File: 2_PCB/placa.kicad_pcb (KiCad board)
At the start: 2 copper layers, 37 parts, among them J1 Screw_Terminal_01x02, J2 Conn_01x05_Male, J3 Screw_Terminal_01x02, SW1 SW_Push, U1 STM32L051C8Tx, U2 Ai-Thinker-Ra-01, Y1 8 MHz, Y2 32.768 kHz

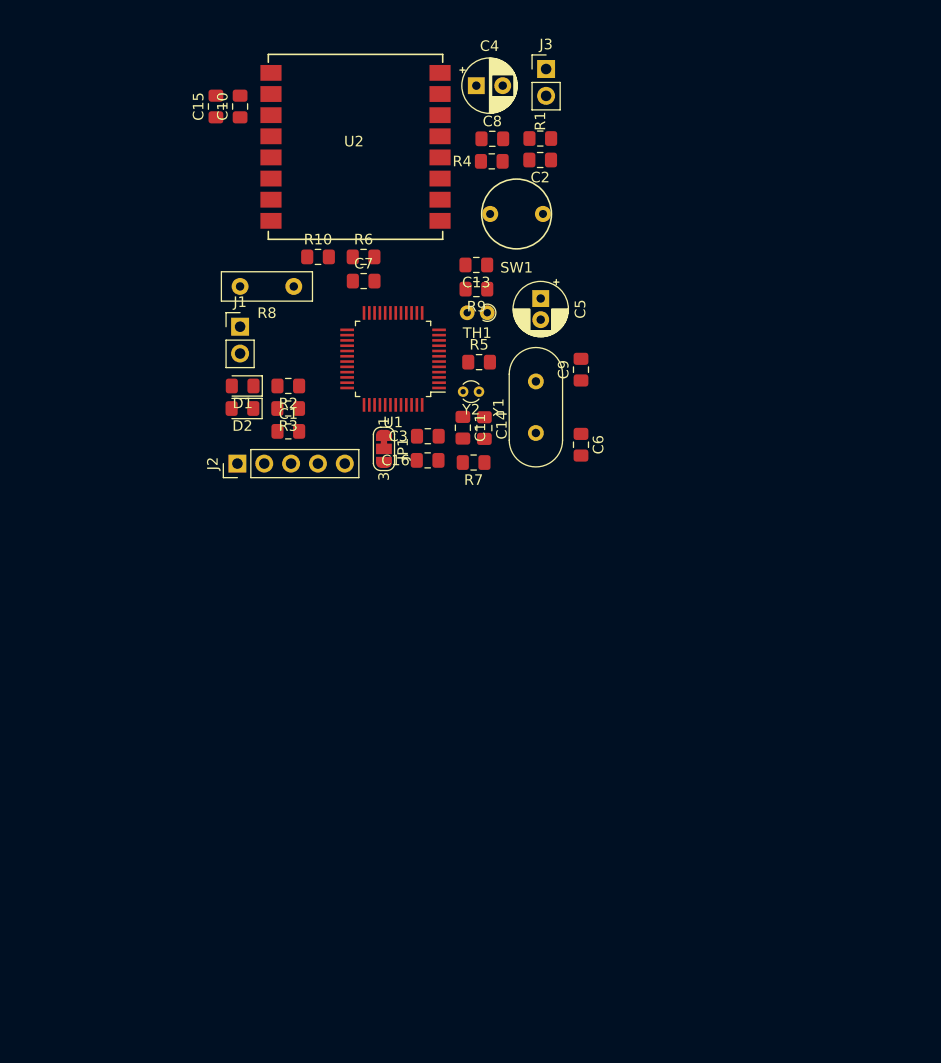
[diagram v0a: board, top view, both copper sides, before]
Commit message: Remap SPI pins, reposition components; start routing
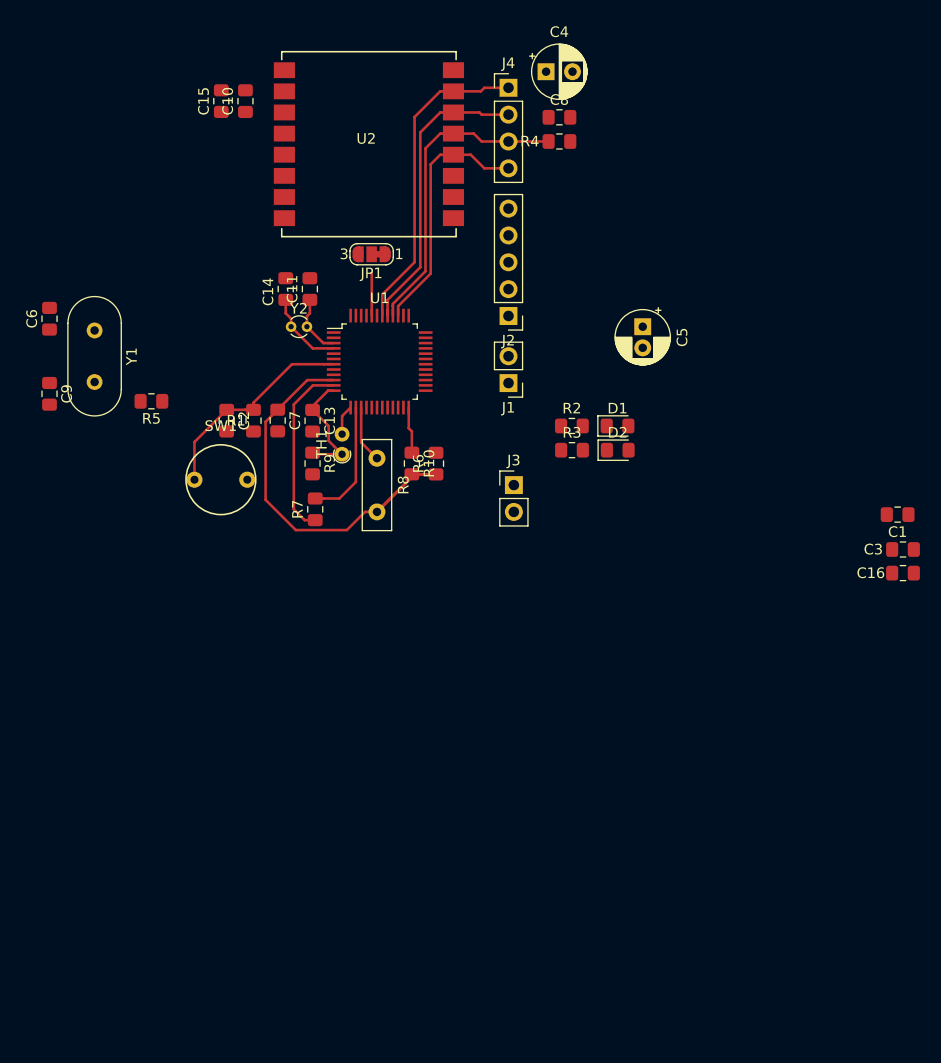
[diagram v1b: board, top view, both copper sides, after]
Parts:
- added J4: TestPoints, Connector_PinHeader_2.54mm:PinHeader_1x04_P2.54mm_Vertical, F.Cu at (138.7, 32.3)
- moved C1 58.2 mm to (175.5, 72.6), turned to 180 degrees
- moved C6 51.7 mm to (95.2, 54.1), turned to 90 degrees
- moved C9 50.3 mm to (95.2, 61.2), turned to 270 degrees
- moved C16 46.2 mm to (176.0, 78.2)
- moved C3 46.2 mm to (176.0, 75.9)
- moved Y1 42.9 mm to (99.5, 55.2), turned to 270 degrees
- moved J3 39.5 mm to (139.2, 69.8)
- moved C2 38.6 mm to (112.0, 63.8), turned to 270 degrees
- moved R1 38.1 mm to (114.6, 63.8), turned to 90 degrees
- moved SW1 37.6 mm to (111.5, 69.3), turned to 180 degrees
- moved D2 35.7 mm to (149.0, 66.5), turned to 0 degrees
- moved D1 35.7 mm to (149.0, 64.3), turned to 0 degrees
- moved R5 31.2 mm to (104.9, 61.9), turned to 180 degrees
- moved J2 29.2 mm to (138.7, 53.8), turned to 180 degrees
- moved R3 27.1 mm to (144.7, 66.5), turned to 0 degrees
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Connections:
- J2 pad 3: /SWCLK -> /NRST
- J2 pad 4: /NRST -> /SWCLK
- U1 pad 10: /ADC_TEMP -> /ADC_RH
- U1 pad 12: /ADC_RH -> /ADC_TEMP
- U1 pad 15: /SPI_SCK -> /PWR_RH
- U1 pad 16: /SPI_MISO -> (no net)
- U1 pad 17: /SPI_MOSI -> (no net)
- U1 pad 18: /SPI_CS -> (no net)
- U1 pad 19: /LoRa_Reset -> (no net)
- U1 pad 2: Net-(U1-Pad2) -> /LoRa_Reset
- U1 pad 20: /PWR_RH -> (no net)
- U1 pad 21: Net-(U1-Pad21) -> (no net)
- U1 pad 22: Net-(U1-Pad22) -> (no net)
- U1 pad 25: Net-(U1-Pad25) -> (no net)
- U1 pad 26: Net-(U1-Pad26) -> (no net)
- U1 pad 27: Net-(U1-Pad27) -> (no net)
- U1 pad 28: Net-(U1-Pad28) -> (no net)
- U1 pad 29: Net-(U1-Pad29) -> (no net)
- U1 pad 33: Net-(U1-Pad33) -> (no net)
- U1 pad 38: Net-(U1-Pad38) -> (no net)
- U1 pad 39: Net-(U1-Pad39) -> /SPI_SCK
- U1 pad 40: Net-(U1-Pad40) -> /SPI_MISO
- U1 pad 41: Net-(U1-Pad41) -> /SPI_MOSI
- U1 pad 42: Net-(U1-Pad42) -> /SPI_CS
- U1 pad 43: Net-(U1-Pad43) -> (no net)
- U1 pad 45: Net-(U1-Pad45) -> (no net)
- U1 pad 46: Net-(U1-Pad46) -> (no net)
- U2 pad 1: Net-(U2-Pad1) -> (no net)
- U2 pad 10: Net-(U2-Pad10) -> (no net)
- U2 pad 11: Net-(U2-Pad11) -> (no net)
- U2 pad 5: Net-(U2-Pad5) -> (no net)
- U2 pad 6: Net-(U2-Pad6) -> (no net)
- U2 pad 7: Net-(U2-Pad7) -> (no net)
- U2 pad 8: Net-(U2-Pad8) -> (no net)
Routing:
- net /ADC_RH: track 0.00 -> 35.1 mm
- net /SPI_CS: track 0.00 -> 30.1 mm
- net /SPI_MISO: track 0.00 -> 29.6 mm
- net /SPI_MOSI: track 0.00 -> 28.3 mm
- net /SPI_SCK: track 0.00 -> 23.9 mm
- net /NRST: track 0.00 -> 20.2 mm
- net /ADC_MS: track 0.00 -> 16.9 mm
- net /PWR_MS: track 0.00 -> 11.5 mm
- net /ADC_TEMP: track 0.00 -> 11.2 mm
- net /RCC_OSC32_OUT: track 0.00 -> 7.63 mm
- net /RCC_OSC32_IN: track 0.00 -> 5.83 mm
- net /PWR_RH: track 0.00 -> 5.41 mm
- net VCC: track 0.00 -> 4.39 mm
- net Net-(JP1-Pad2): track 0.00 -> 4.04 mm
- net /PWR_TEMP: track 0.00 -> 2.85 mm
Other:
- net class Default: clearance 0.2 -> 0.24; via_drill 0.4 -> 0.6
- rule trace_clearance: 0.2 -> 0.24
- rule trace_min: 0.2 -> 0.25
- rule via_min_drill: 0.3 -> 0.6
- rule via_min_size: 0.4 -> 0.8

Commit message: Finished first iteration of PCB
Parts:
- U2: footprint RF_Module:Ai-Thinker-Ra-01-LoRa -> TCC:Ai-Thinker-Ra-01-LoRa
- moved C16 47.0 mm to (130.3, 67.3)
- moved C3 46.9 mm to (130.3, 65.3)
- moved C1 43.4 mm to (134.8, 57.7)
- moved C5 42.8 mm to (111.5, 39.4), turned to 0 degrees
- moved J3 40.3 mm to (107.6, 44.8), turned to 180 degrees
- moved C8 34.5 mm to (112.3, 49.8), turned to 270 degrees
- moved C4 30.9 mm to (120.1, 52.3), turned to 90 degrees
- moved D2 15.7 mm to (134.1, 71.4), turned to 270 degrees
- moved D1 14.7 mm to (136.1, 71.4), turned to 270 degrees
- moved C6 12.3 mm to (106.9, 50.2), turned to 180 degrees
- moved C9 11.7 mm to (106.2, 65.5)
- moved R3 10.6 mm to (134.1, 66.0), turned to 270 degrees
- moved R4 9.51 mm to (138.6, 29.2), turned to 180 degrees
- moved R2 8.72 mm to (136.1, 66.0), turned to 270 degrees
- moved Y1 8.44 mm to (108.0, 54.9)
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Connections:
- U1 pad 25: (no net) -> /userLED
- U1 pad 32: /userLED -> (no net)
- U2 pad 1: (no net) -> Net-(U2-Pad1)
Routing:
- net VCC: track 4.39 -> 110.7 mm, vias 0 -> 1
- net /NRST: track 20.2 -> 81.3 mm
- net /LoRa_Reset: track 0.00 -> 24.8 mm, vias 0 -> 2
- net /RCC_OSC_IN: track 0.00 -> 20.4 mm
- net /SWCLK: track 0.00 -> 13.0 mm
- net /SWDIO: track 0.00 -> 9.96 mm
- net GND: track 0.00 -> 9.89 mm, vias 0 -> 7
- net /RCC_OSC_OUT: track 0.00 -> 9.73 mm
- net /UART_TX: track 0.00 -> 9.42 mm
- net Net-(C9-Pad1): track 0.00 -> 8.69 mm
- net /UART_RX: track 0.00 -> 8.58 mm
- net Net-(JP1-Pad2): track 4.04 -> 11.9 mm
- net /userLED: track 0.00 -> 7.39 mm
- net /SPI_MISO: track 29.6 -> 35.2 mm
- net Net-(D2-Pad1): track 0.00 -> 3.30 mm
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- added copper zone on B.Cu, net GND
- added copper zone on F.Cu, net GND

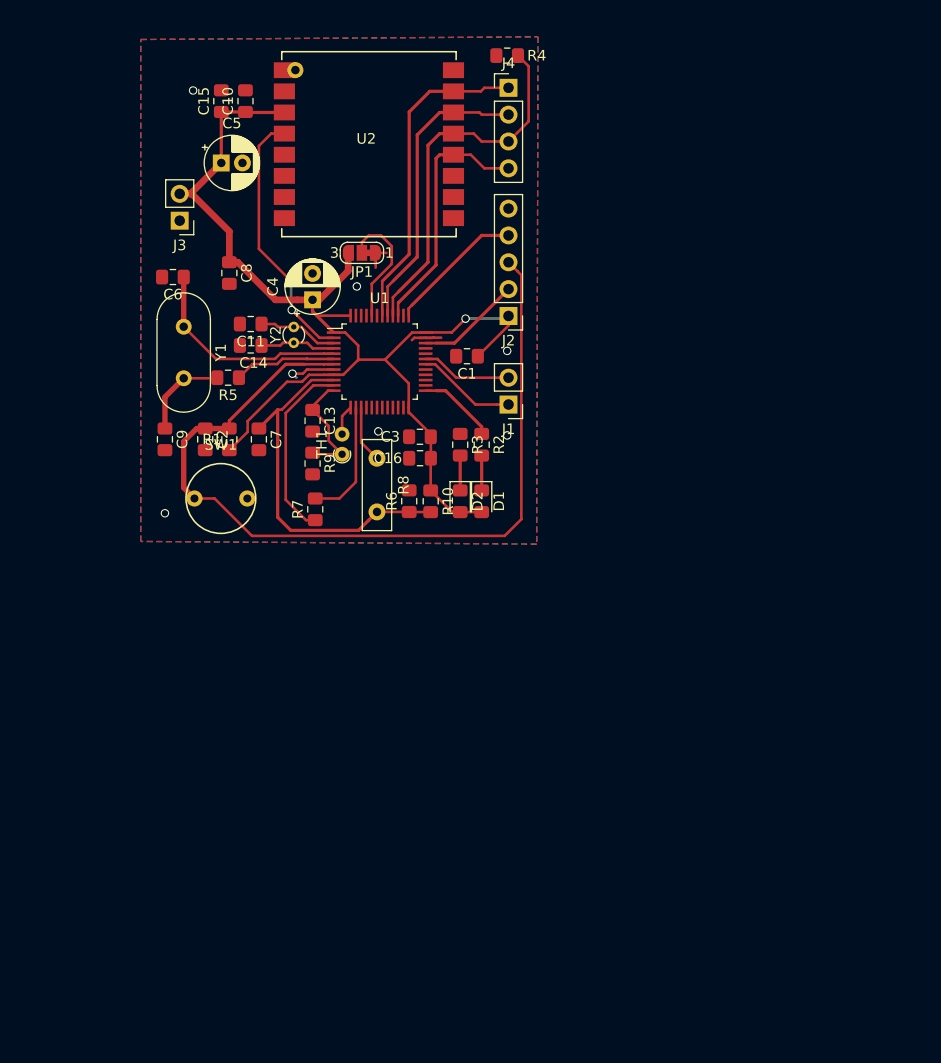
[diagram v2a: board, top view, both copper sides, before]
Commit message: Created and added capacitive sensor to PCB; Minor changes to the design
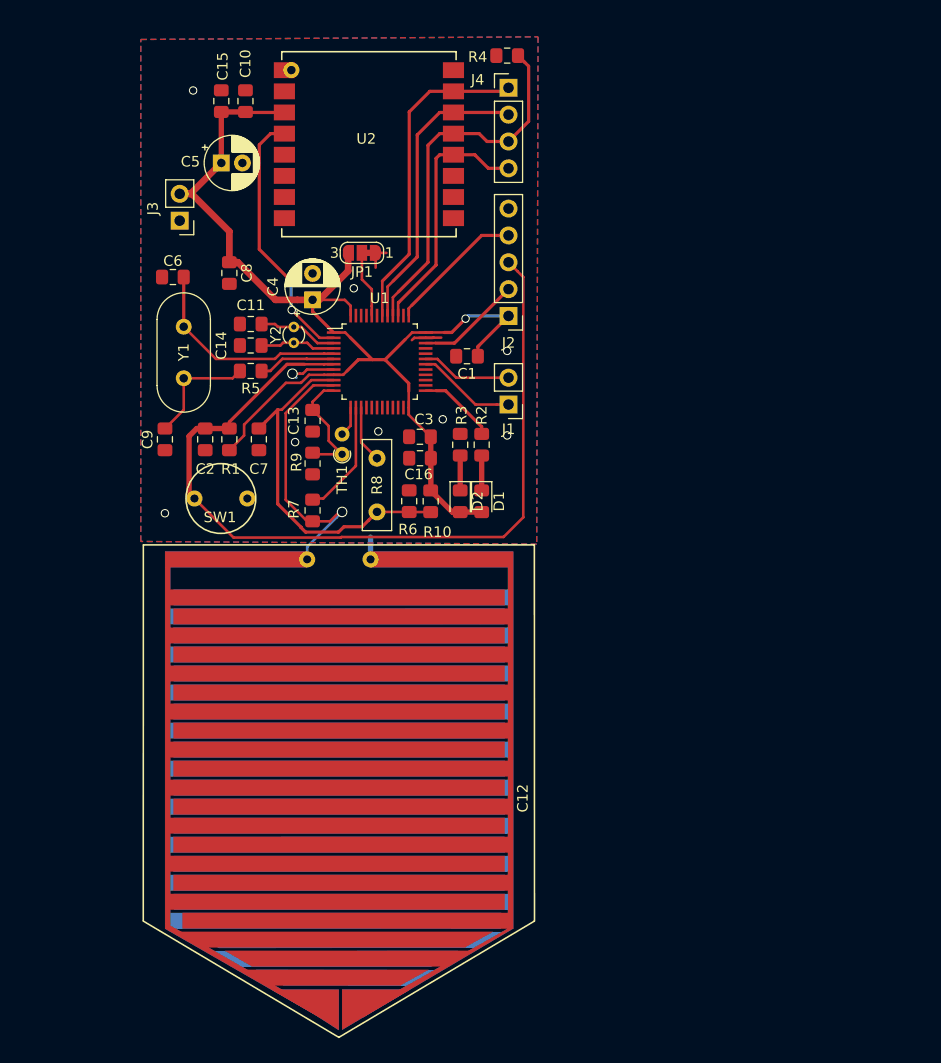
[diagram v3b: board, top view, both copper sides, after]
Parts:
- added C12: C_Variable, TCC:Moisture Sensor, F.Cu at (121.0, 100.7)
- moved R5 2.23 mm to (114.3, 59.1)
- moved R7 0.28 mm to (120.1, 72.3)
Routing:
- net /ADC_MS: track 17.4 -> 26.4 mm, vias 0 -> 1
- net Net-(JP1-Pad2): track 11.9 -> 6.32 mm
- net /RCC_OSC_OUT: track 9.73 -> 7.31 mm
- net Net-(C9-Pad1): track 8.69 -> 11.1 mm
- net GND: track 9.89 -> 12.0 mm, vias 7 -> 9
- net /PWR_MS: track 11.5 -> 10.6 mm
- net /ADC_RH: track 34.9 -> 34.3 mm
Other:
- net class Default: via_dia 0.8 -> 1; via_drill 0.6 -> 0.8

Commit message: Got LaTeX doc working according to ABNT. Uploaded simulation files of the moisture sensor capacitor. Small changes to the board
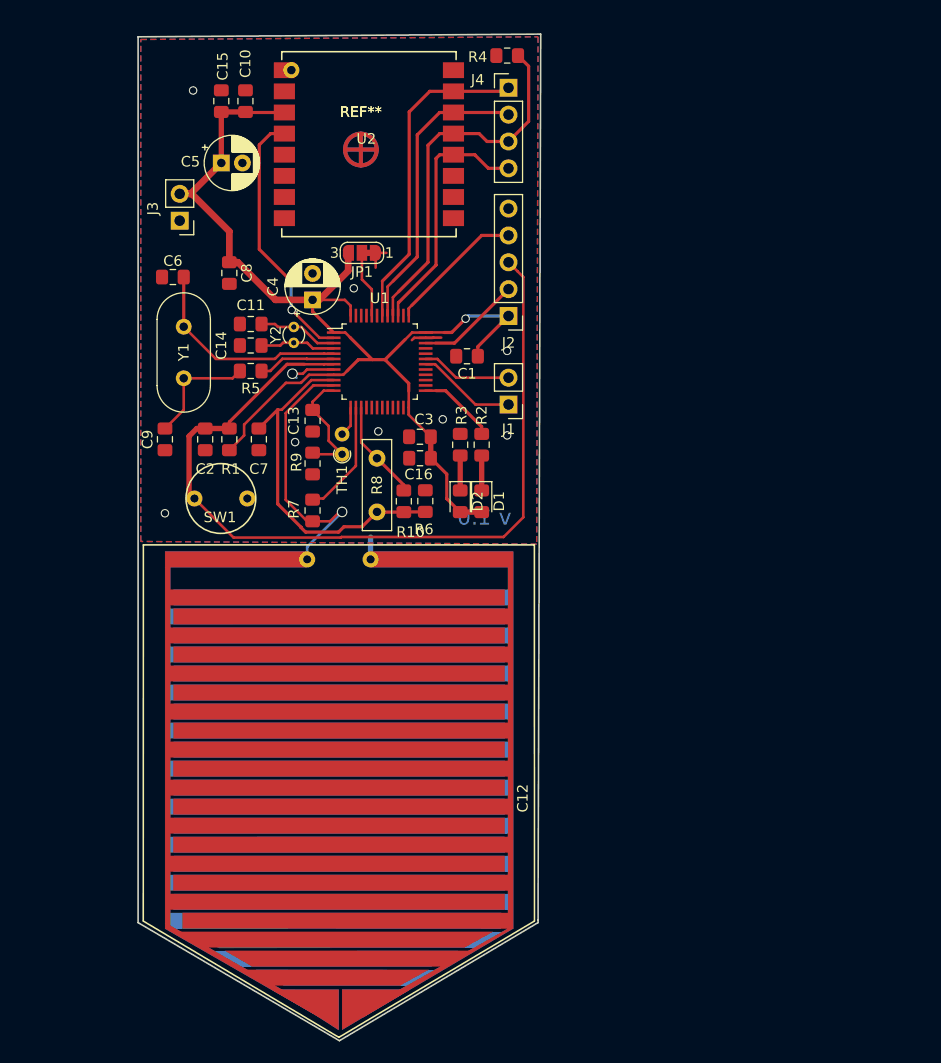
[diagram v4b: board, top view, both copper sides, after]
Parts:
- added REF**: Fiducial_classic_Small_CopperTop_Type1, Fiducial:Fiducial_classic_Small_CopperTop_Type1, F.Cu at (124.7, 38.1)
- added REF**: Fiducial_classic_Small_CopperBottom_Type1, Fiducial:Fiducial_classic_Small_CopperBottom_Type1, F.Cu at (124.7, 38.1)
- moved R10 2.54 mm to (128.8, 71.4)
- moved R6 1.52 mm to (130.8, 71.4)
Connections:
- R10 pad 1: VCC -> /PWR_RH
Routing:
- net /PWR_RH: track 5.41 -> 9.51 mm
- net /ADC_RH: track 34.3 -> 33.8 mm
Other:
- board outline added: 38.1 x 95.2 mm
- board text added: "v 1.0"

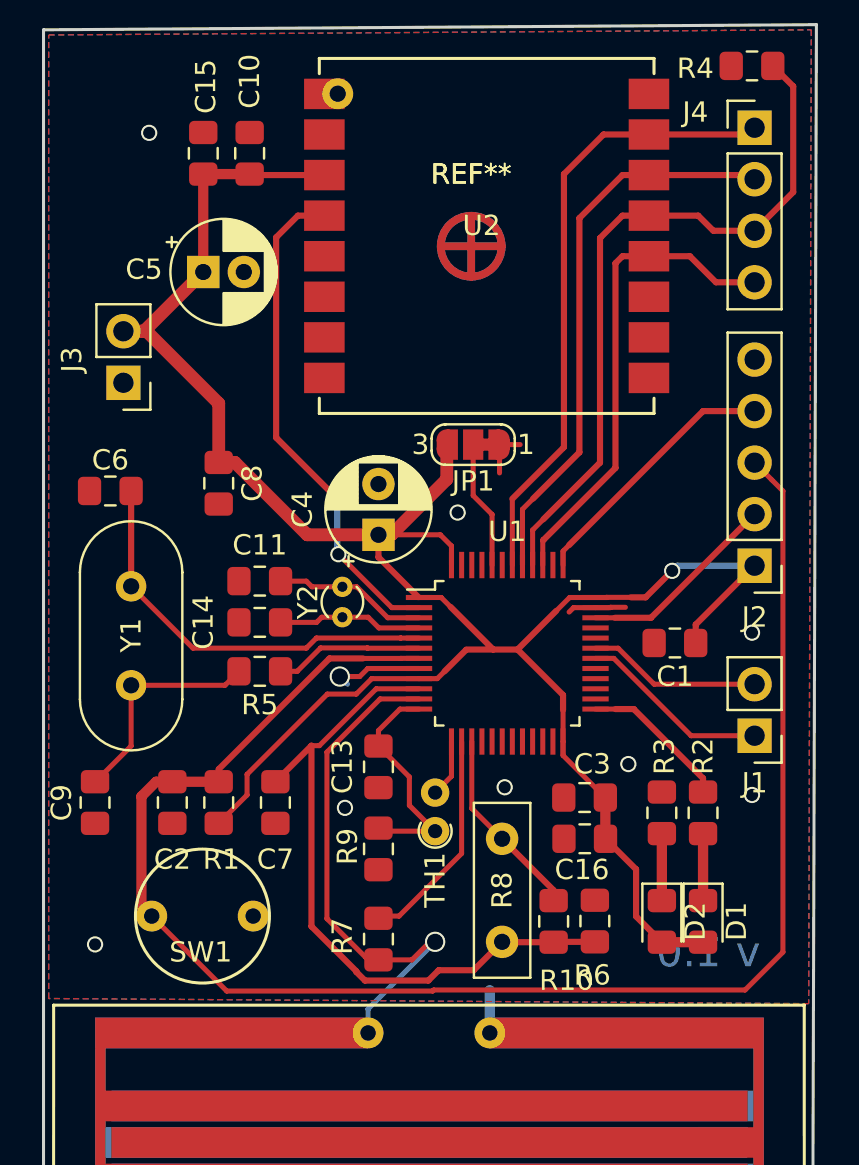
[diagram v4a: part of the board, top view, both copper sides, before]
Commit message: Version 1.01 of PCB (easier for home etch). Chapter one of document
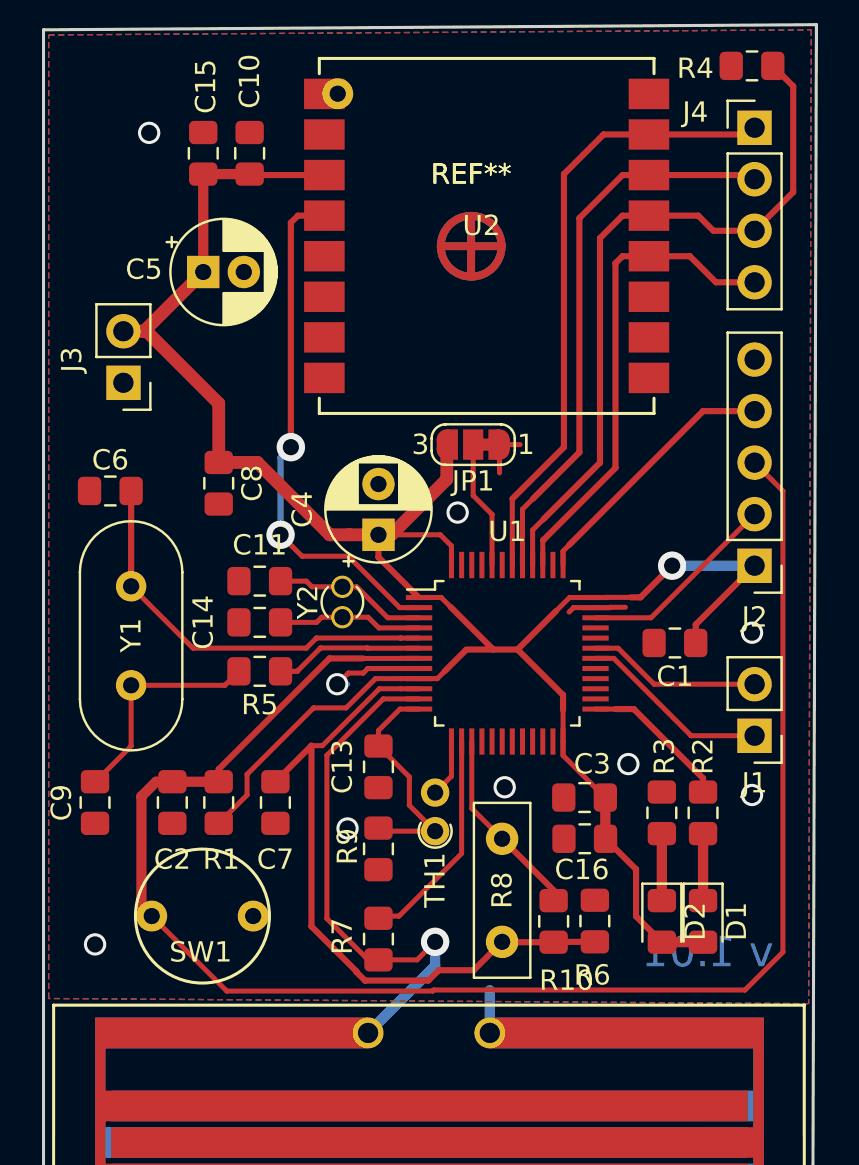
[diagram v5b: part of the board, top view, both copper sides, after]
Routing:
- net /LoRa_Reset: track 24.8 -> 25.7 mm
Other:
- net class Default: via_dia 1 -> 1.1
- rule via_min_drill: 0.6 -> 0.8
- rule via_min_size: 0.8 -> 1.1
- board text added: "v 1.01"
- board text removed: "v 1.0"
